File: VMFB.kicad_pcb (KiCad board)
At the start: 2 copper layers, 154.1 x 111.9 mm, 136 parts, among them J1 Screw_Terminal_01x02, J10 Conn_01x03_Pin, J11 Conn_01x08_Pin, J12 Conn_01x06_Pin, J13 Conn_01x03_Pin, J14 Conn_01x03_Pin, J15 Conn_01x03_Pin, J16 Conn_01x03_Pin, J17 Conn_01x03_Pin, J18 Conn_01x03_Pin, J19 Conn_01x02_Pin, J2 USB_A_Stacked, J20 Conn_01x03_Pin, J21 Conn_01x02_Pin, J3 USB_B, J4 Barrel_Jack_Switch, J5 Conn_01x02_Pin, J6 Conn_01x03_Pin, J7 Conn_01x02_Pin, J8 Conn_01x03_Pin, J9 Conn_01x03_Pin, Q1 BC547B, Q2 TIP41C, Q3 BC547B, Q4 BC547B, Q5 BD139, Q6 BC547B, Q7 BC547B, Q8 BC547, U1 NE555P, U2 NE555P, U3 LM358, U4 NE555P, U5 NE555P

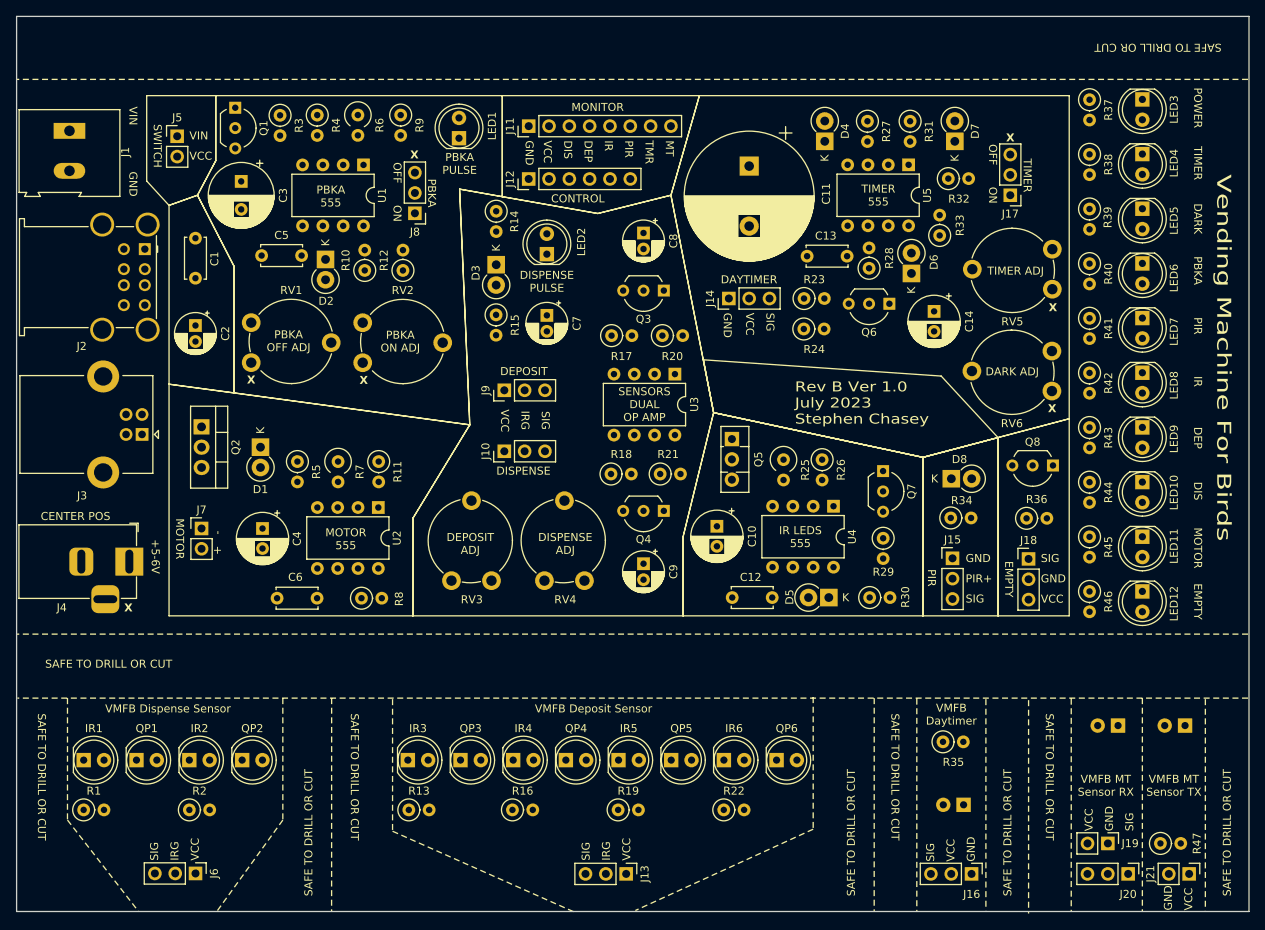
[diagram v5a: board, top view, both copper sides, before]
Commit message: removed transistor/resistor disabline PBKA when IR is on = grounding this along with the IR and signal LEDs instead of using another transistor
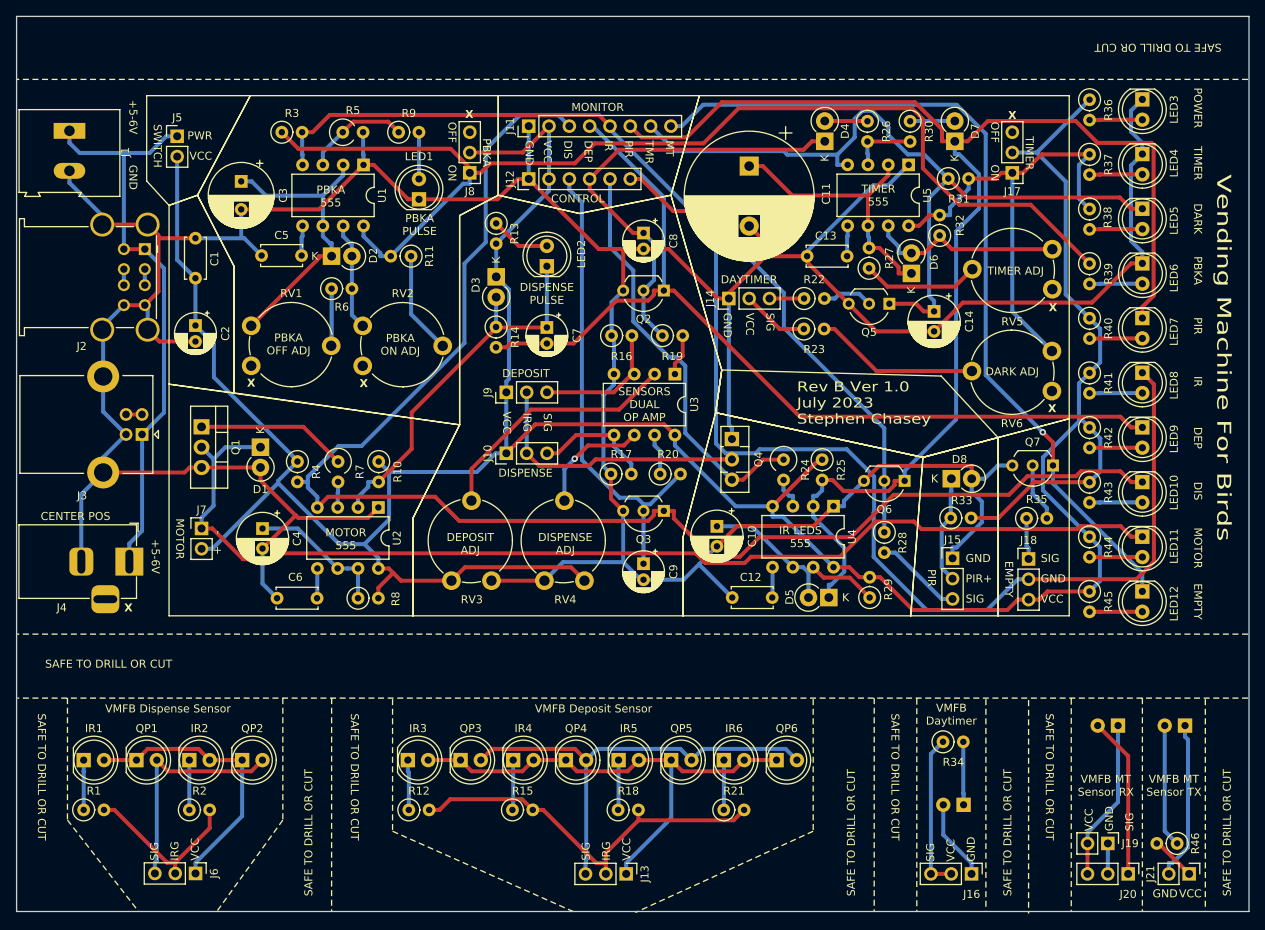
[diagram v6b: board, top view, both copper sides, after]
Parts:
- removed the Q1 at (98.4, 41.1)
- removed the R3 at (104.0, 42.1)
- moved LED1 9.13 mm to (121.4, 52.6)
- moved J8 8.52 mm to (127.8, 49.3)
- moved R3 4.92 mm to (104.3, 44.2), turned to 0 degrees
- moved R6 4.73 mm to (110.5, 63.8), turned to 0 degrees
- moved Q6 2.96 mm to (182.1, 87.8), turned to 180 degrees
- moved R5 2.86 mm to (111.9, 44.2), turned to 0 degrees
- moved J17 2.81 mm to (195.6, 49.3)
- moved R9 2.16 mm to (118.9, 44.2), turned to 0 degrees
- moved R46 2.09 mm to (216.2, 133.1), turned to 180 degrees
- moved R11 2.05 mm to (120.4, 59.7), turned to 180 degrees
- moved C7 1.51 mm to (137.4, 68.6)
- moved LED2 1.51 mm to (137.4, 61.0)
- moved R13 1.51 mm to (131.1, 55.6)
- moved D3 1.51 mm to (131.1, 62.3)
- moved R14 1.51 mm to (131.0, 68.5)
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- renumbered Q2 to Q1, Q3 to Q2, Q4 to Q3, Q5 to Q4, Q6 to Q5, Q7 to Q6, Q8 to Q7, R11 to R10, R12 to R11, R13 to R12, R14 to R13, R15 to R14, R16 to R15, R17 to R16, R18 to R17, R19 to R18, R20 to R19, R21 to R20, R22 to R21, R23 to R22, R24 to R23, R25 to R24, R26 to R25, R27 to R26, R28 to R27, R29 to R28, R30 to R29, R4 to R3, R31 to R30, R32 to R31, R33 to R32, R34 to R33, R35 to R34, R36 to R35, R37 to R36, R38 to R37, R39 to R38, R40 to R39, R5 to R4, R41 to R40, R42 to R41, R43 to R42, R44 to R43, R45 to R44, R46 to R45, R47 to R46, R6 to R5, R10 to R6
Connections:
- R11 pad 1: Net-(R12-Pad1) -> Net-(R11-Pad1)
- R11 pad 2: Net-(D2-A) -> Net-(J8-Pin_1)
- R3 pad 2: Net-(Q2-C) -> IR GND
- RV2 pad 2: Net-(J8-Pin_1) -> Net-(R11-Pad1)
- RV2 pad 3: Net-(R12-Pad1) -> Net-(D2-A)
- U1 pad 4: Net-(Q2-C) -> IR GND
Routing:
- net GND: track 0.00 -> 487.1 mm
- net VCC: track 0.00 -> 392.3 mm
- net IR GND: track 0.00 -> 220.7 mm
- net MOTOR RESET: track 0.00 -> 183.9 mm
- net PIR MON: track 0.00 -> 172.8 mm
- net Net-(D1-K): track 0.00 -> 141.1 mm
- net Net-(J8-Pin_1): track 0.00 -> 139.6 mm
- net DEPOSIT MON: track 0.00 -> 115.8 mm
- net EMPTY MON: track 0.00 -> 107.3 mm, vias 0 -> 1
- net TIMER MON: track 0.00 -> 98.6 mm
- net Net-(J1-Pin_1): track 0.00 -> 72.8 mm
- net Net-(IR3-A): track 0.00 -> 63.6 mm
- net PIR CON/MON: track 0.00 -> 60.2 mm, vias 0 -> 1
- net Net-(J17-Pin_1): track 0.00 -> 59.9 mm
- net DISPENSE CON/MON: track 0.00 -> 59.4 mm
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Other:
- board text added: "PWR"
- board text removed: "VIN"

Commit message: small tweaks and corrected 'Deposit Pulse' LED label (was 'Dispense Pulse')
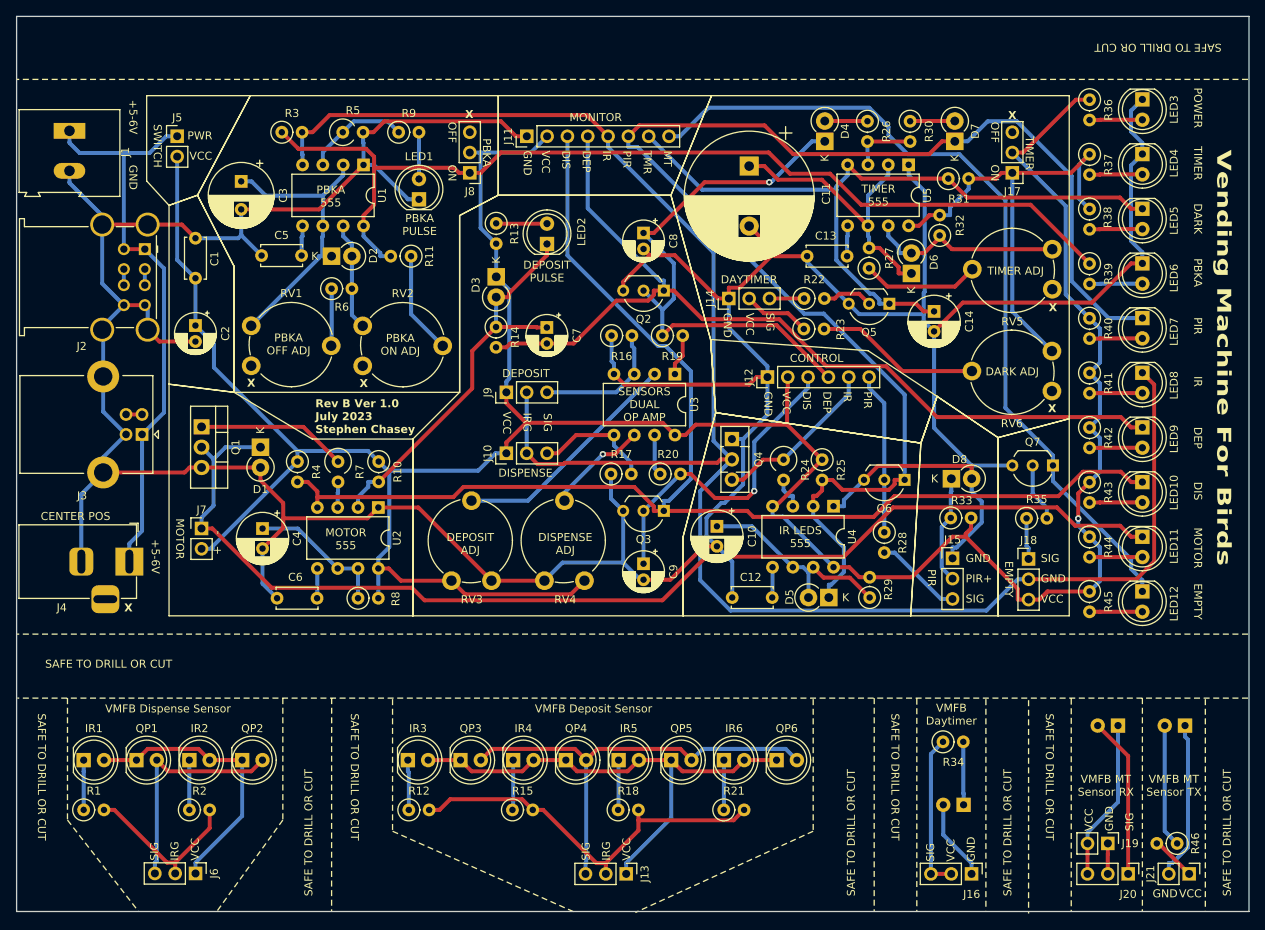
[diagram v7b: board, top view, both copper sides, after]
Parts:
- moved J12 38.8 mm to (165.0, 74.8)
- moved LED2 2.78 mm to (137.4, 58.2)
- moved J11 1.29 mm to (134.9, 44.7)
- moved Q6 0.13 mm to (182.1, 87.7)
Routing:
- net PIR CON/MON: track 60.2 -> 20.2 mm, vias 1 -> 0
- net IR CON/MON: track 51.9 -> 21.2 mm
- net GND: track 487.1 -> 515.7 mm
- net VCC: track 392.3 -> 368.8 mm, vias 0 -> 1
- net DISPENSE CON/MON: track 59.4 -> 41.0 mm, vias 0 -> 1
- net Net-(J8-Pin_1): track 139.6 -> 124.5 mm
- net MOTOR RESET: track 183.9 -> 168.9 mm
- net DEPOSIT CON/MON: track 56.5 -> 69.8 mm, vias 0 -> 1
- net IR GND: track 220.7 -> 227.0 mm
- net TIMER MON: track 98.6 -> 93.0 mm
- net Net-(D1-K): track 141.1 -> 145.5 mm
- net MOTOR TRIGGER: track 48.2 -> 50.8 mm
- net EMPTY MON: track 107.3 -> 104.9 mm, vias 1 -> 0
- net DEPOSIT ADJ: track 31.8 -> 29.4 mm
- net PIR MON: track 172.8 -> 174.9 mm
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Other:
- board text added: "DEPOSIT PULSE"
- board text removed: "DISPENSE PULSE"

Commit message: added transistor to the PBKA
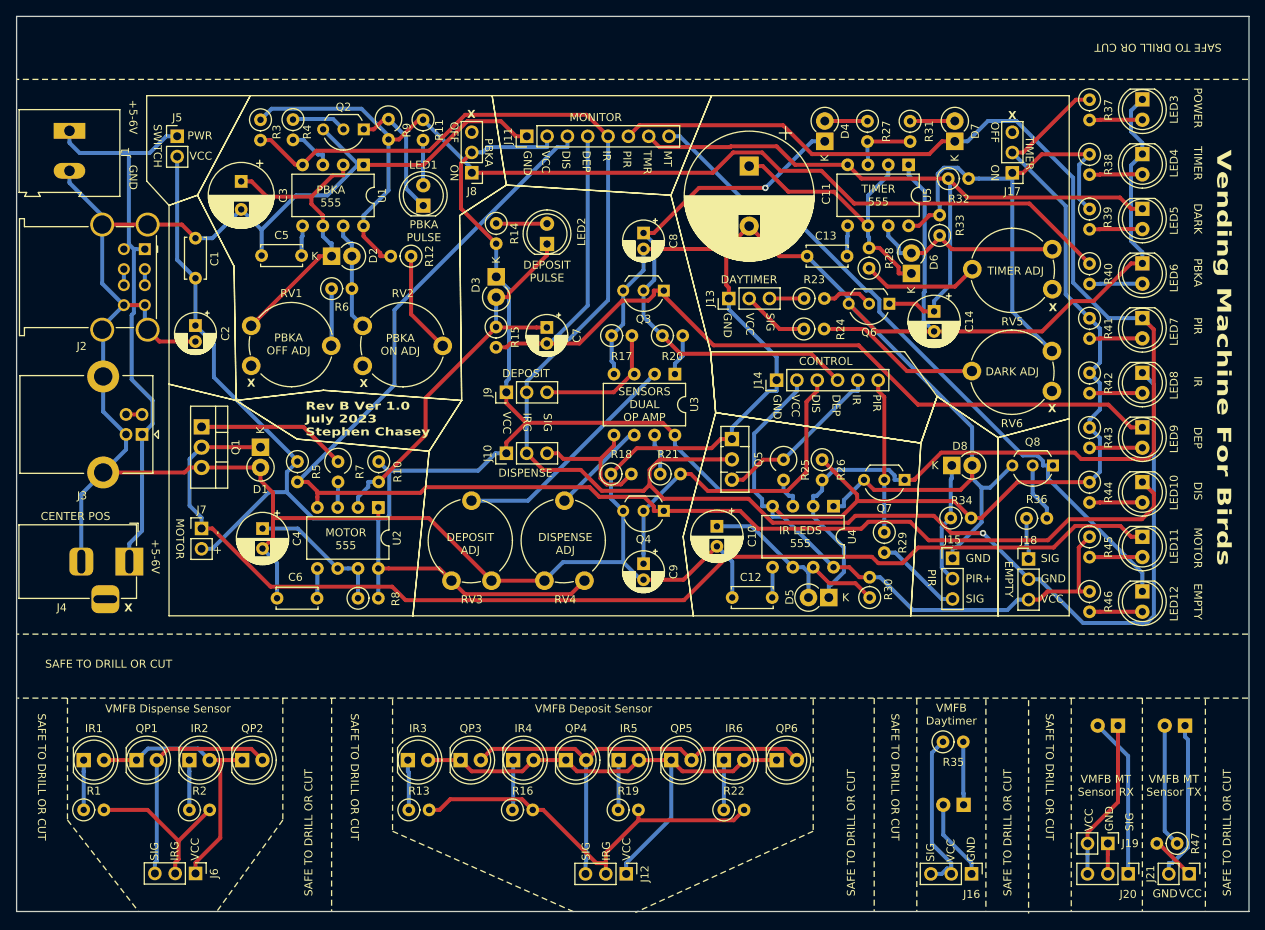
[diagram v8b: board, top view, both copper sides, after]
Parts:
- removed the R5 at (111.9, 44.2)
- added Q2: BC337, Package_TO_SOT_THT:TO-92_Inline_Wide, F.Cu at (114.5, 43.8)
- added R11: 10K, Resistor_THT:R_Axial_DIN0207_L6.3mm_D2.5mm_P2.54mm_Vertical, F.Cu at (121.9, 42.6)
- added R4: 2.2K, Resistor_THT:R_Axial_DIN0207_L6.3mm_D2.5mm_P2.54mm_Vertical, F.Cu at (105.7, 42.6)
- R9: value 10K -> 47R; footprint Resistor_THT:R_Axial_DIN0207_L6.3mm_D2.5mm_P2.54mm_Vertical -> Resistor_THT:R_Axial_DIN0309_L9.0mm_D3.2mm_P2.54mm_Vertical
- moved R3 3.09 mm to (101.6, 42.6), turned to -90 degrees
- moved R9 2.07 mm to (117.6, 42.6), turned to -90 degrees
- moved D8 1.66 mm to (188.0, 85.9)
- moved J14 1.20 mm to (166.1, 75.2)
- moved LED1 0.95 mm to (121.9, 53.4)
- moved J8 0.25 mm to (128.0, 49.3)
- renumbered J13 to J12, J14 to J13, J12 to J14, Q2 to Q3, Q3 to Q4, Q4 to Q5, Q5 to Q6, Q6 to Q7, Q7 to Q8, R11 to R12, R12 to R13, R13 to R14, R14 to R15, R15 to R16, R16 to R17, R17 to R18, R18 to R19, R19 to R20, R20 to R21, R21 to R22, R22 to R23, R23 to R24, R24 to R25, R25 to R26, R26 to R27, R27 to R28, R28 to R29, R29 to R30, R30 to R31, R31 to R32, R32 to R33, R33 to R34, R34 to R35, R35 to R36, R36 to R37, R37 to R38, R38 to R39, R39 to R40, R40 to R41, R41 to R42, R42 to R43, R43 to R44, R44 to R45, R45 to R46, R46 to R47, R4 to R5
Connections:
- LED1 pad 1: GND -> Net-(LED1-K)
- R9 pad 1: Net-(U1-Q) -> Net-(LED1-K)
- R9 pad 2: Net-(LED1-A) -> Net-(J8-Pin_1)
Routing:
- net VCC: track 368.8 -> 409.3 mm, vias 1 -> 0
- net EMPTY MON: track 104.9 -> 86.9 mm
- net Net-(LED1-K): track 0.00 -> 16.2 mm
- net Net-(J8-Pin_1): track 124.5 -> 135.0 mm
- net PIR MON: track 174.9 -> 166.3 mm
- net MOTOR RESET: track 168.9 -> 177.0 mm
- net Net-(U1-Q): track 13.2 -> 5.79 mm
- net Net-(Q2-B): track 0.00 -> 6.87 mm
- net DEPOSIT MON: track 114.6 -> 120.0 mm
- net GND: track 515.7 -> 510.7 mm
- net TIMER MON: track 93.0 -> 89.0 mm
- net DEPOSIT CON/MON: track 69.8 -> 66.5 mm
- net Net-(J17-Pin_1): track 59.9 -> 62.8 mm
- net DISPENSE: track 15.1 -> 17.8 mm
- net IR GND: track 227.0 -> 224.9 mm, vias 0 -> 1
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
